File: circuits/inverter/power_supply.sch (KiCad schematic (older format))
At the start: 0 parts

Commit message: Add more circuitry, add library content
AC current measurement
AC filter
AC switch
DC booster
DC input
Analog frontend
drivers
inverter
main controller
power supply

new components for:
standard library (e.g. relay)
AC current sensor acs722
voltage regulator LM317L

Footprints for:
AC relay
TO-220
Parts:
- added C?: 100n, symbol Capacitor
- added C?: 1µ/6.3V, symbol Capacitor
- added D?: 1N4148, symbol Diode
- added R?: 1650, symbol Resistor
- added R?: 1000, symbol Resistor
- added U?: LM317L, symbol LM317L
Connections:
- net labels added: +15V, +3V3, DC_Link_Vtg, GND
- wire segments 0 -> 18
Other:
- note added: "I_max = 100 mA"
- note added: "V_out = V_ref × (1 + R2÷R1) + (I_adj × R2)\n = 1.25 V × (1 + 1650 Ω÷1000 Ω) + (50 µA × 1650 Ω)\n = 3,395 V"
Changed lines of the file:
@@
 EESchema Schematic File Version 2
+LIBS:lm317
 LIBS:kv30f
 LIBS:OSSI_standard_components
@@
 LIBS:lm4030
 LIBS:power
+LIBS:acs722
 LIBS:OSSI_MK_I-cache
 EELAYER 25 0
@@
 $Descr A4 11693 8268
 encoding utf-8
-Sheet 1 10
-Title ""
-Date ""
+Sheet 10 11
+Title "Power Supply"
+Date "2016-03-17"
 Rev "0.1"
 Comp "Open Source Solar Inverter Project"
@@
 Comment4 ""
 $EndDescr
+$Comp
+L Capacitor C?
+U 1 1 56EB37EB
+P 7650 5250
+F 0 "C?" H 7650 5100 60  0000 C CNN
+F 1 "100n" H 7665 5395 60  0000 C CNN
+F 2 "" H 7650 5250 60  0000 C CNN
+F 3 "" H 7650 5250 60  0000 C CNN
+F 4 "%" H 7650 5475 60  0001 C CNN "Tolerance"
+F 5 "M" H 7900 5450 60  0001 L CNN "Manufacturer"
+F 6 "P" H 7900 5350 60  0001 L CNN "Partnumber"
+	1    7650 5250
+	0    -1   1    0
+$EndComp
+$Comp
+L +15V #+15V?
+U 1 1 56EB3891
+P 7650 4850
+F 0 "#+15V?" H 7650 5125 60  0001 C CNN
+F 1 "+15V" H 7650 5050 60  0000 C CNN
+F 2 "" H 7650 4850 60  0000 C CNN
+F 3 "" H 7650 4850 60  0000 C CNN
+	1    7650 4850
+	1    0    0    -1
+$EndComp
+Wire Wire Line
+	7650 4850 7650 5150
+Wire Wire Line
+	7650 5000 8400 5000
+Connection ~ 7650 5000
+$Comp
+L GND #GND?
+U 1 1 56EB38B3
+P 7650 5650
+F 0 "#GND?" H 7650 5350 60  0001 C CNN
+F 1 "GND" H 7650 5500 60  0000 C CNN
+F 2 "" H 7650 5650 60  0000 C CNN
+F 3 "" H 7650 5650 60  0000 C CNN
+	1    7650 5650
+	1    0    0    -1
+$EndComp
+Wire Wire Line
+	7650 5350 7650 5650
+$Comp
+L Resistor R?
+U 1 1 56EB38E3
+P 8000 5550
+F 0 "R?" H 8000 5450 60  0000 C CNN
+F 1 "1650" H 8000 5550 60  0000 C CNN
+F 2 "" H 8000 5640 60  0001 R CNN
+F 3 "" H 8000 5550 60  0000 C CNN
+F 4 "1%" H 8000 5650 60  0000 C CNN "Tolerance"
+F 5 "M" H 8175 5750 60  0001 L CNN "Manufacturer"
+F 6 "P" H 8175 5650 60  0001 L CNN "Partnumber"
+	1    8000 5550
+	1    0    0    -1
+$EndComp
+$Comp
+L Resistor R?
+U 1 1 56EB3945
+P 9050 5550
+F 0 "R?" H 9050 5450 60  0000 C CNN
+F 1 "1000" H 9050 5550 60  0000 C CNN
+F 2 "" H 9050 5640 60  0001 R CNN
+F 3 "" H 9050 5550 60  0000 C CNN
+F 4 "1%" H 9050 5650 60  0000 C CNN "Tolerance"
+F 5 "M" H 9225 5750 60  0001 L CNN "Manufacturer"
+F 6 "P" H 9225 5650 60  0001 L CNN "Partnumber"
+	1    9050 5550
+	1    0    0    -1
+$EndComp
+$Comp
+L Diode D?
+U 1 1 56EB39FF
+P 8800 4600
+F 0 "D?" H 8800 4475 60  0000 C CNN
+F 1 "1N4148" H 8800 4725 60  0000 C CNN
+F 2 "" H 8775 4600 60  0000 C CNN
+F 3 "" H 8775 4600 60  0000 C CNN
+F 4 "M" H 8975 4800 60  0001 L CNN "Manufacturer"
+F 5 "P" H 8975 4700 60  0001 L CNN "Partnumber"
+	1    8800 4600
+	-1   0    0    -1
+$EndComp
+Wire Wire Line
+	7750 5550 7650 5550
+Connection ~ 7650 5550
+Wire Wire Line
+	8250 5550 8800 5550
+Connection ~ 8350 5550
+$Comp
+L Capacitor C?
+U 1 1 56EB3A73
+P 10000 5250
+F 0 "C?" H 10000 5100 60  0000 C CNN
+F 1 "1µ/6.3V" H 10015 5395 60  0000 C CNN
+F 2 "" H 10000 5250 60  0000 C CNN
+F 3 "" H 10000 5250 60  0000 C CNN
+F 4 "%" H 10000 5475 60  0001 C CNN "Tolerance"
+F 5 "M" H 10250 5450 60  0001 L CNN "Manufacturer"
+F 6 "P" H 10250 5350 60  0001 L CNN "Partnumber"
+	1    10000 5250
+	0    -1   1    0
+$EndComp
+$Comp
+L GND #GND?
+U 1 1 56EB3AF8
+P 10000 5650
+F 0 "#GND?" H 10000 5350 60  0001 C CNN
+F 1 "GND" H 10000 5500 60  0000 C CNN
+F 2 "" H 10000 5650 60  0000 C CNN
+F 3 "" H 10000 5650 60  0000 C CNN
+	1    10000 5650
+	1    0    0    -1
+$EndComp
+Wire Wire Line
+	10000 5650 10000 5350
+Wire Wire Line
+	9200 5000 10000 5000
+Wire Wire Line
+	10000 4850 10000 5150
+$Comp
+L +3V3 #+3V3?
+U 1 1 56EB3B1C
+P 10000 4850
+F 0 "#+3V3?" H 10000 5125 60  0001 C CNN
+F 1 "+3V3" H 10000 5050 60  0000 C CNN
+F 2 "" H 10000 4850 60  0000 C CNN
+F 3 "" H 10000 4850 60  0000 C CNN
+	1    10000 4850
+	1    0    0    -1
+$EndComp
+Connection ~ 10000 5000
+Wire Wire Line
+	9350 5300 9200 5300
+Wire Wire Line
+	9350 4600 9350 5550
+Connection ~ 9350 5000
+Wire Wire Line
+	9200 5100 9350 5100
+Connection ~ 9350 5100
+Wire Wire Line
+	9200 5200 9350 5200
+Connection ~ 9350 5200
+Connection ~ 9350 5300
+Wire Wire Line
+	8400 5300 8350 5300
+Wire Wire Line
+	8350 5300 8350 5550
+Text Notes 7500 6200 0    60   ~ 0
+V_out = V_ref × (1 + R2÷R1) + (I_adj × R2)\n      = 1.25 V × (1 + 1650 Ω÷1000 Ω) + (50 µA × 1650 Ω)\n      = 3,395 V
+Wire Wire Line
+	8600 4600 8200 4600
+Wire Wire Line
+	8200 4600 8200 5000
+Connection ~ 8200 5000
+Wire Wire Line
+	9000 4600 9350 4600
+Text Notes 10050 4900 0    60   ~ 0
+I_max = 100 mA
+Wire Wire Line
+	9350 5550 9300 5550
+$Comp
+L LM317L U?
+U 1 1 56EBF05B
+P 8800 5150
+F 0 "U?" H 8800 4900 60  0000 C CNN
+F 1 "LM317L" H 8800 5400 60  0000 C CNN
+F 2 "" H 8800 5150 60  0000 C CNN
+F 3 "" H 8800 5150 60  0000 C CNN
+F 4 "M" H 9050 5550 60  0001 L CNN "Manufacturer"
+F 5 "P" H 9050 5450 60  0001 L CNN "Partnumber"
+F 6 "Place copper area on pins 2,3,6,7" H 9050 5650 50  0001 L CNN "Comment"
+	1    8800 5150
+	1    0    0    -1
+$EndComp
+Text HLabel 1250 800  0    60   Input ~ 0
+DC_Link_Vtg
 $EndSCHEMATC

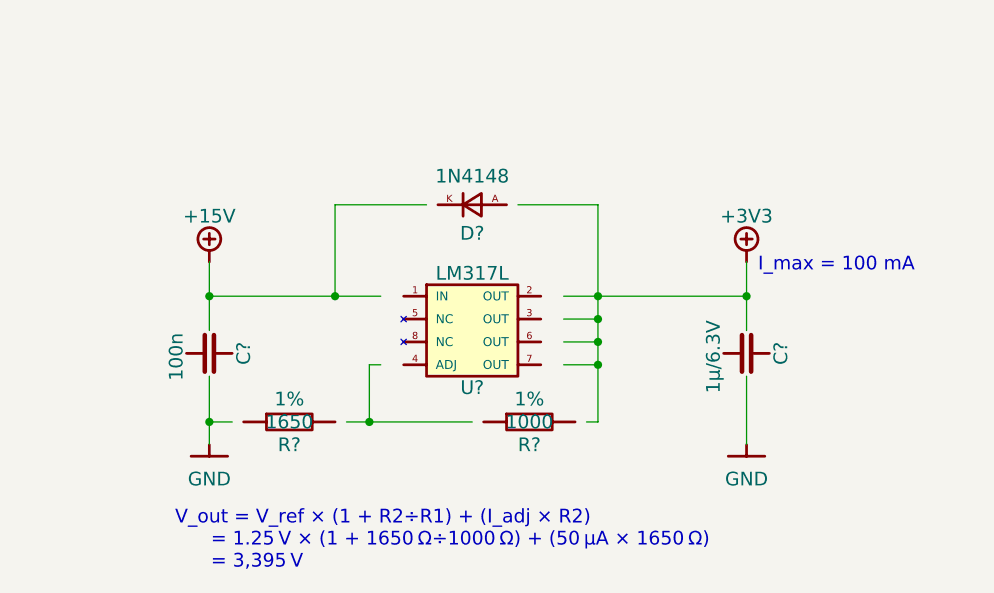
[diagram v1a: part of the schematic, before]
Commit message: Updates all schematic pages to current components
all components are replaced with the current component library parts
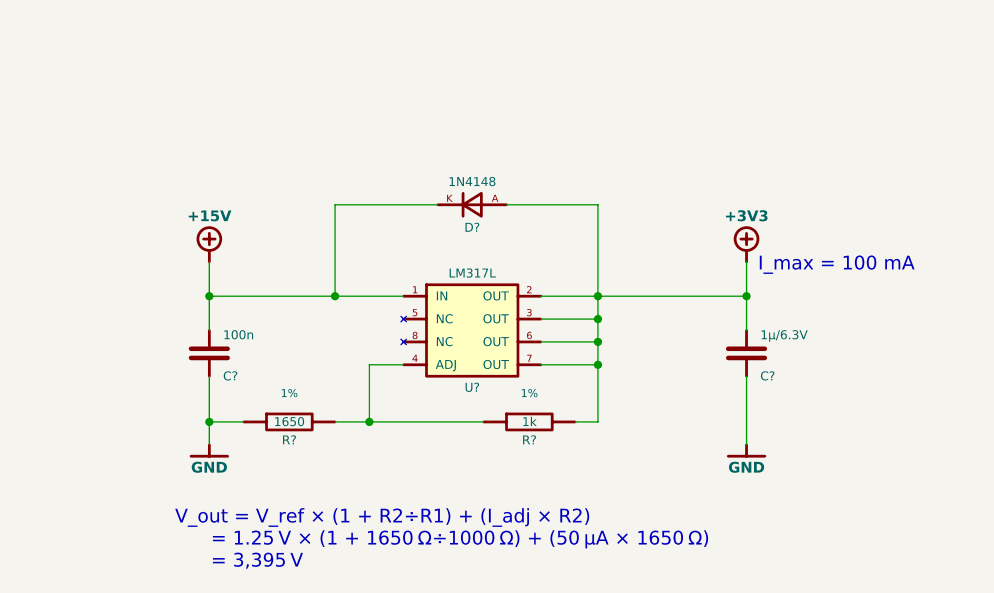
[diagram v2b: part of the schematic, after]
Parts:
- removed C?: 100n, symbol Capacitor
- removed C?: 1µ/6.3V, symbol Capacitor
- removed D?: 1N4148, symbol Diode
- removed R?: 1650, symbol Resistor
- removed R?: 1000, symbol Resistor
- removed U?: LM317L, symbol LM317L
- added C?: 100n, symbol Capacitor
- added C?: 1µ/6.3V, symbol Capacitor
- added D?: 1N4148, symbol Diode
- added R?: 1650, symbol Resistor
- added R?: 1k, symbol Resistor
- added U?: LM317L, symbol LM317L
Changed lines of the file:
@@
 LIBS:connectors
 LIBS:lm4030
-LIBS:power
 LIBS:acs722
 LIBS:OSSI_MK_I-cache
@@
 Comment4 ""
 $EndDescr
+Wire Wire Line
+	7650 4850 7650 5150
+Wire Wire Line
+	7650 5000 8500 5000
+Connection ~ 7650 5000
+Wire Wire Line
+	7650 5350 7650 5650
+Wire Wire Line
+	7650 5550 7800 5550
+Connection ~ 7650 5550
+Wire Wire Line
+	8200 5550 8850 5550
+Connection ~ 8350 5550
+Wire Wire Line
+	10000 5650 10000 5350
+Wire Wire Line
+	9100 5000 10000 5000
+Wire Wire Line
+	10000 4850 10000 5150
+Connection ~ 10000 5000
+Wire Wire Line
+	9100 5300 9350 5300
+Wire Wire Line
+	9350 5550 9350 4600
+Connection ~ 9350 5000
+Wire Wire Line
+	9100 5100 9350 5100
+Connection ~ 9350 5100
+Wire Wire Line
+	9100 5200 9350 5200
+Connection ~ 9350 5200
+Connection ~ 9350 5300
+Wire Wire Line
+	8350 5300 8500 5300
+Wire Wire Line
+	8350 5300 8350 5550
+Text Notes 7500 6200 0    60   ~ 0
+V_out = V_ref × (1 + R2÷R1) + (I_adj × R2)\n      = 1.25 V × (1 + 1650 Ω÷1000 Ω) + (50 µA × 1650 Ω)\n      = 3,395 V
+Wire Wire Line
+	8200 4600 8650 4600
+Wire Wire Line
+	8200 4600 8200 5000
+Connection ~ 8200 5000
+Wire Wire Line
+	9350 4600 8950 4600
+Text Notes 10050 4900 0    60   ~ 0
+I_max = 100 mA
+Wire Wire Line
+	9250 5550 9350 5550
+Text HLabel 1250 800  0    60   Input ~ 0
+DC_Link_Vtg
 $Comp
 L Capacitor C?
-U 1 1 56EB37EB
+U 1 1 58DE136E
 P 7650 5250
-F 0 "C?" H 7650 5100 60  0000 C CNN
-F 1 "100n" H 7665 5395 60  0000 C CNN
-F 2 "" H 7650 5250 60  0000 C CNN
-F 3 "" H 7650 5250 60  0000 C CNN
-F 4 "%" H 7650 5475 60  0001 C CNN "Tolerance"
-F 5 "M" H 7900 5450 60  0001 L CNN "Manufacturer"
-F 6 "P" H 7900 5350 60  0001 L CNN "Partnumber"
+F 0 "C?" H 7710 5150 39  0000 L CNN
+F 1 "100n" H 7710 5330 39  0000 L CNN
+F 2 "" H 7600 5160 39  0001 R CNN
+F 3 "" V 7650 5250 60  0000 C CNN
+F 4 "%" H 7600 5330 39  0001 R CNN "Tolerance"
+F 5 "M" H 7710 5445 35  0001 L CNN "Manufacturer"
+F 6 "P" H 7710 5390 35  0001 L CNN "Partnumber"
+F 7 "S" H 7710 5505 35  0001 L CNN "Supplier"
+F 8 "O.No." H 7710 5555 35  0001 L CNN "Order No."
 	1    7650 5250
-	0    -1   1    0
+	1    0    0    -1
+$EndComp
+$Comp
+L Resistor R?
+U 1 1 58DE1602
+P 8000 5550
+F 0 "R?" H 8000 5470 39  0000 C CNN
+F 1 "1650" H 8000 5550 39  0000 C CNN
+F 2 "" H 8000 5620 35  0000 C CNN
+F 3 "" H 8000 5550 60  0000 C CNN
+F 4 "1%" H 8000 5675 35  0000 C CNN "Tolerance"
+F 5 "M" H 8125 5675 35  0001 L CNN "Manufacturer"
+F 6 "P" H 8125 5625 35  0001 L CNN "Partnumber"
+F 7 "S" H 8125 5725 35  0001 L CNN "Supplier"
+F 8 "O.No." H 8125 5775 35  0001 L CNN "Order No."
+	1    8000 5550
+	1    0    0    -1
+$EndComp
+$Comp
+L Resistor R?
+U 1 1 58DE17CC
+P 9050 5550
+F 0 "R?" H 9050 5470 39  0000 C CNN
+F 1 "1k" H 9050 5550 39  0000 C CNN
+F 2 "" H 9050 5620 35  0000 C CNN
+F 3 "" H 9050 5550 60  0000 C CNN
+F 4 "1%" H 9050 5675 35  0000 C CNN "Tolerance"
+F 5 "M" H 9175 5675 35  0001 L CNN "Manufacturer"
+F 6 "P" H 9175 5625 35  0001 L CNN "Partnumber"
+F 7 "S" H 9175 5725 35  0001 L CNN "Supplier"
+F 8 "O.No." H 9175 5775 35  0001 L CNN "Order No."
+	1    9050 5550
+	1    0    0    -1
+$EndComp
+$Comp
+L LM317L U?
+U 1 1 58DE1946
+P 8800 5150
+F 0 "U?" H 8800 4900 39  0000 C CNN
+F 1 "LM317L" H 8800 5400 39  0000 C CNN
+F 2 "" H 8800 5150 60  0000 C CNN
+F 3 "" H 8800 5150 60  0000 C CNN
+F 4 "M" H 8950 5450 35  0001 L CNN "Manufacturer"
+F 5 "P" H 8950 5400 35  0001 L CNN "Partnumber"
+F 6 "S" H 8950 5500 35  0001 L CNN "Supplier"
+F 7 "O.No." H 8950 5550 35  0001 L CNN "Order No."
+	1    8800 5150
+	1    0    0    -1
+$EndComp
+$Comp
+L Diode D?
+U 1 1 58DE1C2A
+P 8800 4600
+F 0 "D?" H 8800 4500 39  0000 C CNN
+F 1 "1N4148" H 8800 4700 39  0000 C CNN
+F 2 "" H 8785 4600 60  0000 C CNN
+F 3 "" H 8785 4600 60  0000 C CNN
+F 4 "M" H 8975 4760 35  0001 L CNN "Manufacturer"
+F 5 "P" H 8975 4700 35  0001 L CNN "Partnumber"
+F 6 "S" H 8975 4815 35  0001 L CNN "Supplier"
+F 7 "O.No." H 8975 4870 35  0001 L CNN "Order No."
+	1    8800 4600
+	-1   0    0    -1
+$EndComp
+$Comp
+L Capacitor C?
+U 1 1 58DE1E08
+P 10000 5250
+F 0 "C?" H 10060 5150 39  0000 L CNN
+F 1 "1µ/6.3V" H 10060 5330 39  0000 L CNN
+F 2 "" H 9950 5160 39  0001 R CNN
+F 3 "" V 10000 5250 60  0000 C CNN
+F 4 "%" H 9950 5330 39  0001 R CNN "Tolerance"
+F 5 "M" H 10060 5445 35  0001 L CNN "Manufacturer"
+F 6 "P" H 10060 5390 35  0001 L CNN "Partnumber"
+F 7 "S" H 10060 5505 35  0001 L CNN "Supplier"
+F 8 "O.No." H 10060 5555 35  0001 L CNN "Order No."
+	1    10000 5250
+	1    0    0    -1
+$EndComp
+$Comp
+L +3V3 #+3V3?
+U 1 1 58DE1EB7
+P 10000 4850
+F 0 "#+3V3?" H 10000 5125 60  0001 C CNN
+F 1 "+3V3" H 10000 5050 47  0000 C CNB
+F 2 "" H 10000 4850 60  0000 C CNN
+F 3 "" H 10000 4850 60  0000 C CNN
+	1    10000 4850
+	1    0    0    -1
 $EndComp
 $Comp
 L +15V #+15V?
-U 1 1 56EB3891
+U 1 1 58DE1FD8
 P 7650 4850
 F 0 "#+15V?" H 7650 5125 60  0001 C CNN
-F 1 "+15V" H 7650 5050 60  0000 C CNN
+F 1 "+15V" H 7650 5050 47  0000 C CNB
 F 2 "" H 7650 4850 60  0000 C CNN
 F 3 "" H 7650 4850 60  0000 C CNN
@@
 	1    0    0    -1
 $EndComp
-Wire Wire Line
-	7650 4850 7650 5150
-Wire Wire Line
-	7650 5000 8400 5000
-Connection ~ 7650 5000
 $Comp
 L GND #GND?
-U 1 1 56EB38B3
+U 1 1 58DE2057
 P 7650 5650
-F 0 "#GND?" H 7650 5350 60  0001 C CNN
-F 1 "GND" H 7650 5500 60  0000 C CNN
+F 0 "#GND?" H 7650 5460 60  0001 C CNN
+F 1 "GND" H 7650 5550 47  0000 C CNB
 F 2 "" H 7650 5650 60  0000 C CNN
 F 3 "" H 7650 5650 60  0000 C CNN
@@
 	1    0    0    -1
 $EndComp
-Wire Wire Line
-	7650 5350 7650 5650
-$Comp
-L Resistor R?
-U 1 1 56EB38E3
-P 8000 5550
-F 0 "R?" H 8000 5450 60  0000 C CNN
-F 1 "1650" H 8000 5550 60  0000 C CNN
-F 2 "" H 8000 5640 60  0001 R CNN
-F 3 "" H 8000 5550 60  0000 C CNN
-F 4 "1%" H 8000 5650 60  0000 C CNN "Tolerance"
-F 5 "M" H 8175 5750 60  0001 L CNN "Manufacturer"
-F 6 "P" H 8175 5650 60  0001 L CNN "Partnumber"
-	1    8000 5550
-	1    0    0    -1
-$EndComp
-$Comp
-L Resistor R?
-U 1 1 56EB3945
-P 9050 5550
-F 0 "R?" H 9050 5450 60  0000 C CNN
-F 1 "1000" H 9050 5550 60  0000 C CNN
-F 2 "" H 9050 5640 60  0001 R CNN
-F 3 "" H 9050 5550 60  0000 C CNN
-F 4 "1%" H 9050 5650 60  0000 C CNN "Tolerance"
-F 5 "M" H 9225 5750 60  0001 L CNN "Manufacturer"
-F 6 "P" H 9225 5650 60  0001 L CNN "Partnumber"
-	1    9050 5550
-	1    0    0    -1
-$EndComp
-$Comp
-L Diode D?
-U 1 1 56EB39FF
-P 8800 4600
-F 0 "D?" H 8800 4475 60  0000 C CNN
-F 1 "1N4148" H 8800 4725 60  0000 C CNN
-F 2 "" H 8775 4600 60  0000 C CNN
-F 3 "" H 8775 4600 60  0000 C CNN
-F 4 "M" H 8975 4800 60  0001 L CNN "Manufacturer"
-F 5 "P" H 8975 4700 60  0001 L CNN "Partnumber"
-	1    8800 4600
-	-1   0    0    -1
-$EndComp
-Wire Wire Line
-	7750 5550 7650 5550
-Connection ~ 7650 5550
-Wire Wire Line
-	8250 5550 8800 5550
-Connection ~ 8350 5550
-$Comp
-L Capacitor C?
-U 1 1 56EB3A73
-P 10000 5250
-F 0 "C?" H 10000 5100 60  0000 C CNN
-F 1 "1µ/6.3V" H 10015 5395 60  0000 C CNN
-F 2 "" H 10000 5250 60  0000 C CNN
-F 3 "" H 10000 5250 60  0000 C CNN
-F 4 "%" H 10000 5475 60  0001 C CNN "Tolerance"
-F 5 "M" H 10250 5450 60  0001 L CNN "Manufacturer"
-F 6 "P" H 10250 5350 60  0001 L CNN "Partnumber"
-	1    10000 5250
-	0    -1   1    0
-$EndComp
 $Comp
 L GND #GND?
-U 1 1 56EB3AF8
+U 1 1 58DE20A5
 P 10000 5650
-F 0 "#GND?" H 10000 5350 60  0001 C CNN
-F 1 "GND" H 10000 5500 60  0000 C CNN
+F 0 "#GND?" H 10000 5460 60  0001 C CNN
+F 1 "GND" H 10000 5550 47  0000 C CNB
 F 2 "" H 10000 5650 60  0000 C CNN
 F 3 "" H 10000 5650 60  0000 C CNN
@@
 	1    0    0    -1
 $EndComp
-Wire Wire Line
-	10000 5650 10000 5350
-Wire Wire Line
-	9200 5000 10000 5000
-Wire Wire Line
-	10000 4850 10000 5150
-$Comp
-L +3V3 #+3V3?
-U 1 1 56EB3B1C
-P 10000 4850
-F 0 "#+3V3?" H 10000 5125 60  0001 C CNN
-F 1 "+3V3" H 10000 5050 60  0000 C CNN
-F 2 "" H 10000 4850 60  0000 C CNN
-F 3 "" H 10000 4850 60  0000 C CNN
-	1    10000 4850
-	1    0    0    -1
-$EndComp
-Connection ~ 10000 5000
-Wire Wire Line
-	9350 5300 9200 5300
-Wire Wire Line
-	9350 4600 9350 5550
-Connection ~ 9350 5000
-Wire Wire Line
-	9200 5100 9350 5100
-Connection ~ 9350 5100
-Wire Wire Line
-	9200 5200 9350 5200
-Connection ~ 9350 5200
-Connection ~ 9350 5300
-Wire Wire Line
-	8400 5300 8350 5300
-Wire Wire Line
-	8350 5300 8350 5550
-Text Notes 7500 6200 0    60   ~ 0
-V_out = V_ref × (1 + R2÷R1) + (I_adj × R2)\n      = 1.25 V × (1 + 1650 Ω÷1000 Ω) + (50 µA × 1650 Ω)\n      = 3,395 V
-Wire Wire Line
-	8600 4600 8200 4600
-Wire Wire Line
-	8200 4600 8200 5000
-Connection ~ 8200 5000
-Wire Wire Line
-	9000 4600 9350 4600
-Text Notes 10050 4900 0    60   ~ 0
-I_max = 100 mA
-Wire Wire Line
-	9350 5550 9300 5550
-$Comp
-L LM317L U?
-U 1 1 56EBF05B
-P 8800 5150
-F 0 "U?" H 8800 4900 60  0000 C CNN
-F 1 "LM317L" H 8800 5400 60  0000 C CNN
-F 2 "" H 8800 5150 60  0000 C CNN
-F 3 "" H 8800 5150 60  0000 C CNN
-F 4 "M" H 9050 5550 60  0001 L CNN "Manufacturer"
-F 5 "P" H 9050 5450 60  0001 L CNN "Partnumber"
-F 6 "Place copper area on pins 2,3,6,7" H 9050 5650 50  0001 L CNN "Comment"
-	1    8800 5150
-	1    0    0    -1
-$EndComp
-Text HLabel 1250 800  0    60   Input ~ 0
-DC_Link_Vtg
 $EndSCHEMATC

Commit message: bulk-updates libraries and schematics
schematic is updated to Kicad 5.1.14
updates various sheets with new circuits
adds various component libraries
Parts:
- added C?: 2µF/600VDC, symbol OSSI_standard_components:Capacitor
- added C?: 1nF/25V, symbol OSSI_standard_components:Capacitor
- added C?: 220µF/35V, symbol OSSI_standard_components:Capacitor_pol
- added C?: 100nF/50V, symbol OSSI_standard_components:Capacitor
- added C?: 100nF/25V, symbol OSSI_standard_components:Capacitor
- added C? (x2): 100pF, symbol OSSI_standard_components:Capacitor
- added C? (x2): 470µF/35V, symbol OSSI_standard_components:Capacitor_pol
- added D? (x5): Schottky, symbol OSSI_standard_components:Schottky
- added D?: 15V, symbol OSSI_standard_components:Zener
- added D? (x2): 1n4148, symbol OSSI_standard_components:Diode
- added Q?: BC847C, symbol OSSI_standard_components:NPN
- added Q? (x2): AOD1N60, symbol OSSI_standard_components:NMOS
- added Q?: PNP, symbol OSSI_standard_components:PNP
- added R? (x5): 1M, symbol OSSI_standard_components:Resistor
- added R?: 6k8, symbol OSSI_standard_components:Resistor
- added R? (x3): 10k, symbol OSSI_standard_components:Resistor
- added R?: 10Ω, OSSI_standard_footprints:MELF_0204_W, symbol OSSI_standard_components:Resistor
- added R? (x2): 1Ω, OSSI_standard_footprints:MELF_0207_W, symbol OSSI_standard_components:Resistor
- added R?: 2Ω, OSSI_standard_footprints:MELF_0207_W, symbol OSSI_standard_components:Resistor
- added R?: 100Ω, symbol OSSI_standard_components:Resistor
- added R?: 50k, symbol OSSI_standard_components:Resistor
- added T?: TR 15:13, symbol OSSI_standard_components:Transformer
- added U?: UC2845A, symbol UC2845:UC2845A
- C? (x2): symbol Capacitor -> OSSI_standard_components:Capacitor
- D?: symbol Diode -> OSSI_standard_components:Diode
- R? (x2): symbol Resistor -> OSSI_standard_components:Resistor
- U?: symbol LM317L -> lm317:LM317L
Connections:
- net DC_Link_Vtg: now also C?.2, Q?.3 (D), R?.2, T?.1 (Pri1)
- net GND: now reaches C?.1, R?.1
- net GND: now also C?.1, C?.-, C?.-, C?.-, C?.1, C?.1, C?.1, C?.1, C?.1, C?.1, D?.A, Q?.C, Q?.E, R?.1, R?.1, R?.2, R?.2, R?.2, T?.7 (Sec7), U?.5 (GND)
- net +15V: now reaches C?.2, D?.K, U?.1 (IN)
- net +15V: now also C?.+, C?.+, D?.A, D?.A, D?.K, R?.2
- net +3V3: now reaches C?.2, D?.A, R?.2, U?.2 (OUT), U?.3 (OUT), U?.6 (OUT), U?.7 (OUT)
- new net: R?.1, R?.2 (x3)
- new net: Q?.E, U?.1 (Comp)
- new net: C?.2, R?.1, R?.2, U?.2 (VFB)
- new net: C?.2, R?.1, U?.3 (ISENSE)
- new net: C?.2, Q?.B, R?.2, U?.4 (RT/CT)
- new net: D?.A, D?.K, R?.1, U?.6 (OUT)
- new net: C?.+, C?.2, D?.K, D?.K, D?.K, U?.7 (VCC)
- new net: C?.2, R?.1, U?.8 (VREF)
- new net: Q?.1 (G), Q?.C, R?.1
- new net: Q?.B, R?.1
- new net: D?.A, D?.A
- new net: D?.K, D?.K, R?.2, R?.2
- new net: Q?.1 (G), R?.1, R?.2
- new net: Q?.2 (S), R?.1, R?.1, R?.1, R?.2, R?.2
- new net: Q?.3 (D), T?.5 (Pri5)
- new net: D?.A, T?.9 (Sec9)
- new net +15V_startup: D?.A, D?.K, Q?.2 (S)
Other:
- note added: "L_p≈60µH\nT_R 15:13"
- note added: "Provided for output\nnoise protection."
- note added: "Remark: This design is initially derived from TI.com webench Power Designer."
- note added: "Soft Start"
- note added: "disables Startup Voltage Regulator"
- moved on the sheet: C?, D?, R?, U?

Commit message: minor updates and cleaup
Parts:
- D? (x3): footprint (none) -> OSSI_standard_footprints:SOD123_R
- D?: footprint (none) -> OSSI_standard_footprints:SOD123_R; Manufacturer M -> Micro Commercial Co; Partnumber P -> MMSZ5245B
- D? (x2): value 1n4148 -> 1N4148; footprint (none) -> OSSI_standard_footprints:SOD123_R
- D? (x3): value Schottky -> MBR0560; footprint (none) -> OSSI_standard_footprints:SOD123_R
- Q?: footprint (none) -> OSSI_standard_footprints:SOT23_BEC_R
- Q? (x2): footprint (none) -> OSSI_standard_footprints:TO-252-DPAK-GSD
- Q?: value PNP -> BC807; footprint (none) -> OSSI_standard_footprints:SOT23_BEC_R
- R? (x4): footprint (none) -> OSSI_standard_footprints:MELF_0204_W
- U?: footprint (none) -> OSSI_standard_footprints:SOIC8
- U?: Manufacturer (none) -> M; Order No. (none) -> O.No.; Partnumber (none) -> P; Supplier (none) -> S
